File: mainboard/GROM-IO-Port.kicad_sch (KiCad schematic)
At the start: 27 parts, among them J13 I/O Port, J14 GROM Port, U14 74LS00, U15 74LS04, U18 74LS00, U20 74LS04, U3 74LS04, U4 74LS32, U45 74LS244, U46 74LS367, U47 74LS367

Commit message: PCB routed
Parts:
- added J13: I/O Port, Connector_PinHeader_2.54mm:PinHeader_2x22_P2.54mm_Vertical, symbol Connector_Generic:Conn_02x22_Odd_Even
- added J16: GROM Port, Connector_PinHeader_2.54mm:PinHeader_2x18_P2.54mm_Vertical, symbol Connector_Generic:Conn_02x18_Odd_Even
- J14: renamed from J13; footprint (none) -> Library:CardEdge_44Pin_2.54mm_Vertical
- J15: renamed from J14; footprint (none) -> Library:CardEdge_34Pin_2.54mm_Vertical
- U14, U15, U18, U20, U3, U4: footprint Package_DIP:DIP-14_W7.62mm_LongPads -> Package_DIP:DIP-14_W7.62mm_Socket_LongPads
- U44: renamed from U45; footprint Package_DIP:DIP-20_W7.62mm_LongPads -> Package_DIP:DIP-20_W7.62mm_Socket_LongPads
- U45: renamed from U46; footprint Package_DIP:DIP-16_W7.62mm_LongPads -> Package_DIP:DIP-16_W7.62mm_Socket_LongPads
- U46: renamed from U47; footprint Package_DIP:DIP-16_W7.62mm_LongPads -> Package_DIP:DIP-16_W7.62mm_Socket_LongPads
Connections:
- net +5V: now also J13.1 (Pin_1), J16.19 (Pin_19)
- net -5V: now also J13.43 (Pin_43), J16.29 (Pin_29)
- net A10: now also J16.16 (Pin_16)
- net A11: now also J16.14 (Pin_14)
- net A12: now also J16.12 (Pin_12)
- net A13: now also J16.10 (Pin_10)
- net A15-CRUOUT: now also J16.8 (Pin_8)
- net A3: now also J16.24 (Pin_24)
- net A4: now also J16.30 (Pin_30)
- net A5: now also J16.28 (Pin_28)
- net A6: now also J16.26 (Pin_26)
- net A7: now also J16.22 (Pin_22)
- net A8: now also J16.20 (Pin_20)
- net A9: now also J16.18 (Pin_18)
- net CRUIN: now also J16.6 (Pin_6)
- net D0: now also J13.37 (Pin_37), J16.17 (Pin_17)
- net D1: now also J13.40 (Pin_40), J16.15 (Pin_15)
- net D2: now also J13.39 (Pin_39), J16.13 (Pin_13)
- net D3: now also J13.42 (Pin_42), J16.11 (Pin_11)
- net D4: now also J13.35 (Pin_35), J16.9 (Pin_9)
- net D5: now also J13.38 (Pin_38), J16.7 (Pin_7)
- net D6: now also J13.36 (Pin_36), J16.5 (Pin_5)
- net D7: now also J13.34 (Pin_34), J16.3 (Pin_3)
- net DBIN: now also J16.25 (Pin_25)
- net GND: now also J13.21 (Pin_21), J13.23 (Pin_23), J13.25 (Pin_25), J13.27 (Pin_27), J16.2 (Pin_2), J16.35 (Pin_35), J16.36 (Pin_36)
- net GREADY: now also J16.31 (Pin_31)
- net GRMCLK: now also J16.27 (Pin_27)
- net IO_A0: now also J13.31 (Pin_31)
- net IO_A1: now also J13.30 (Pin_30)
- net IO_A10: now also J13.6 (Pin_6)
- net IO_A11: now also J13.8 (Pin_8)
- net IO_A12: now also J13.11 (Pin_11)
- net IO_A13: now also J13.15 (Pin_15)
- net IO_A14: now also J13.16 (Pin_16), J16.23 (Pin_23)
- net IO_A15-CRUOUT: now also J13.19 (Pin_19)
- net IO_A2: now also J13.20 (Pin_20)
- net IO_A3: now also J13.10 (Pin_10)
- net IO_A4: now also J13.7 (Pin_7)
- net IO_A5: now also J13.5 (Pin_5)
- net IO_A6: now also J13.29 (Pin_29)
- net IO_A7: now also J13.17 (Pin_17)
- net IO_A8: now also J13.14 (Pin_14)
- net IO_A9: now also J13.18 (Pin_18)
- net IO_CRUIN: now also J13.33 (Pin_33)
- net IO_DBIN: now also J13.9 (Pin_9)
- net IO_Ø3: now also J13.24 (Pin_24)
- net READY_~{HOLD}: now also J13.12 (Pin_12)
- net SBE: now also J13.2 (Pin_2)
- net VSS: now also J16.33 (Pin_33)
- net ~{CMRESET}: now also J16.1 (Pin_1)
- net ~{CRUCLK}: now also J16.4 (Pin_4)
- net ~{GS}: now also J16.21 (Pin_21)
- net ~{IO_CRUCLK}: now also J13.22 (Pin_22)
- net ~{IO_EXT_INT}: now also J13.4 (Pin_4)
- net ~{IO_LOAD}: now also J13.13 (Pin_13)
- net ~{IO_MBE}: now also J13.28 (Pin_28)
- net ~{IO_RESET}: now also J13.3 (Pin_3)
- net ~{IO_WE}: now also J13.26 (Pin_26)
- net ~{MEMEN}: now also J13.32 (Pin_32)
- net ~{ROMG}: now also J16.34 (Pin_34)
- net ~{mWE}: now also J16.32 (Pin_32)
- net IO_SNDIN: now reaches J14.44 (Pin_44), R103.1
- net IO_SNDIN: now also J13.44 (Pin_44)
- new net HOLD/IAQ: J13.41 (Pin_41)
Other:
- moved on the sheet: U45, U46

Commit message: unicorn work
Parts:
- renumbered R104 to R100, R89 to R85, R90 to R86, R91 to R87, R92 to R88, R93 to R89, R94 to R90, R95 to R91, R96 to R92, R97 to R93, R98 to R94, R99 to R95, R100 to R96, R101 to R97, R102 to R98, R103 to R99, U44 to U40, U45 to U41, U46 to U42

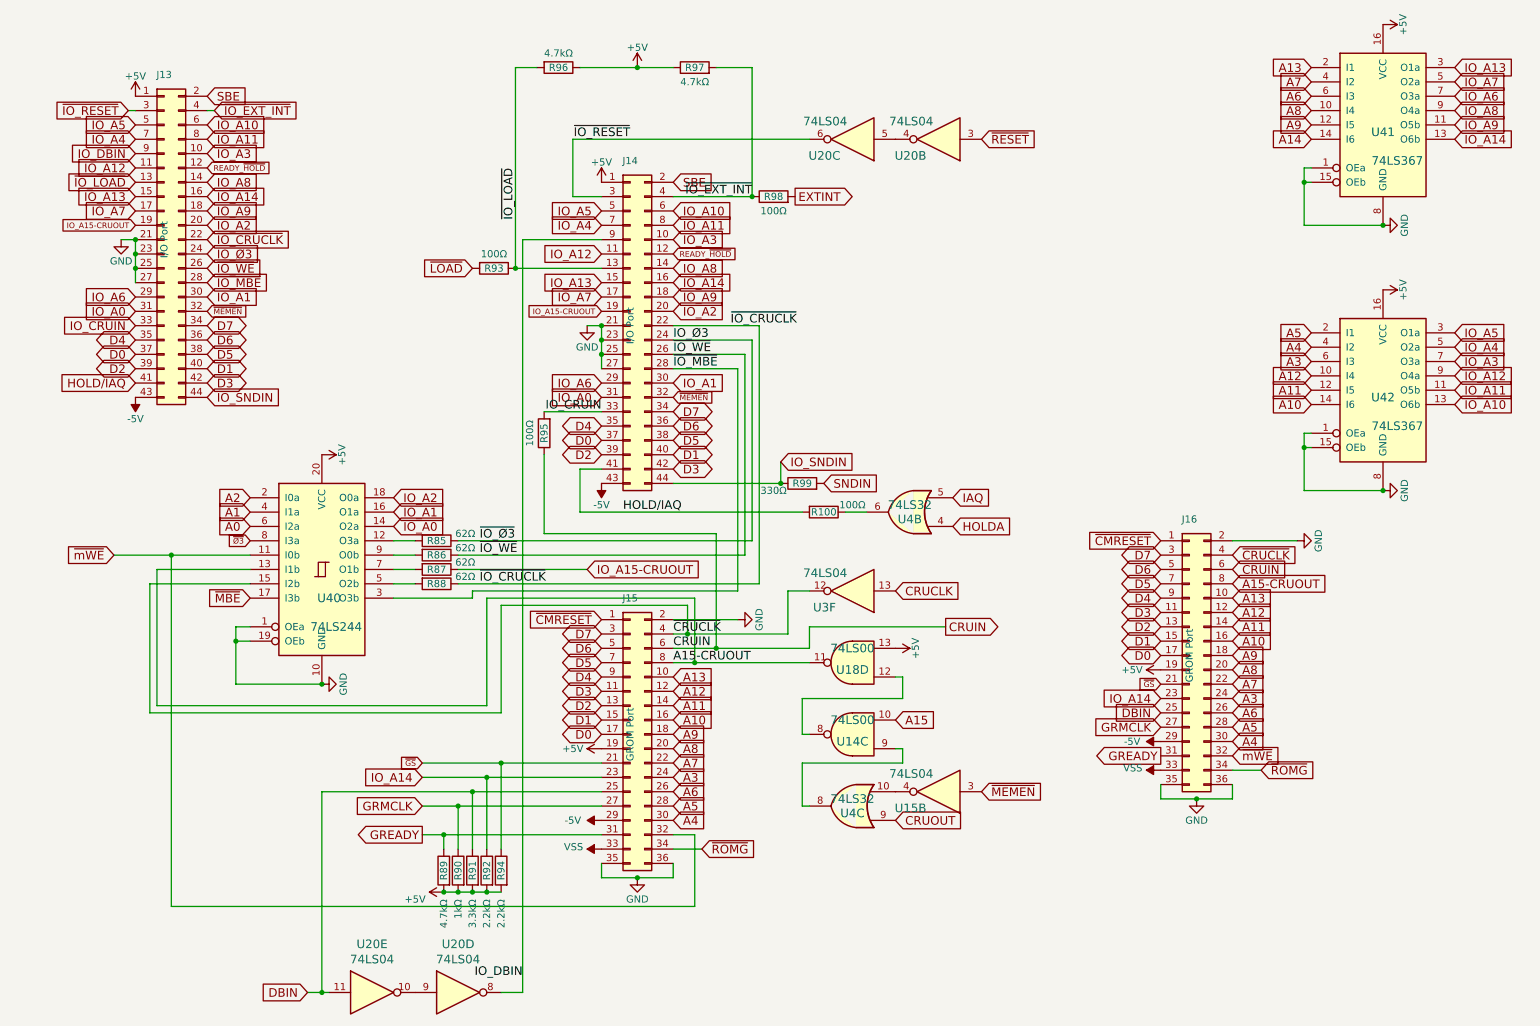
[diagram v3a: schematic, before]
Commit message: Shrink PCB
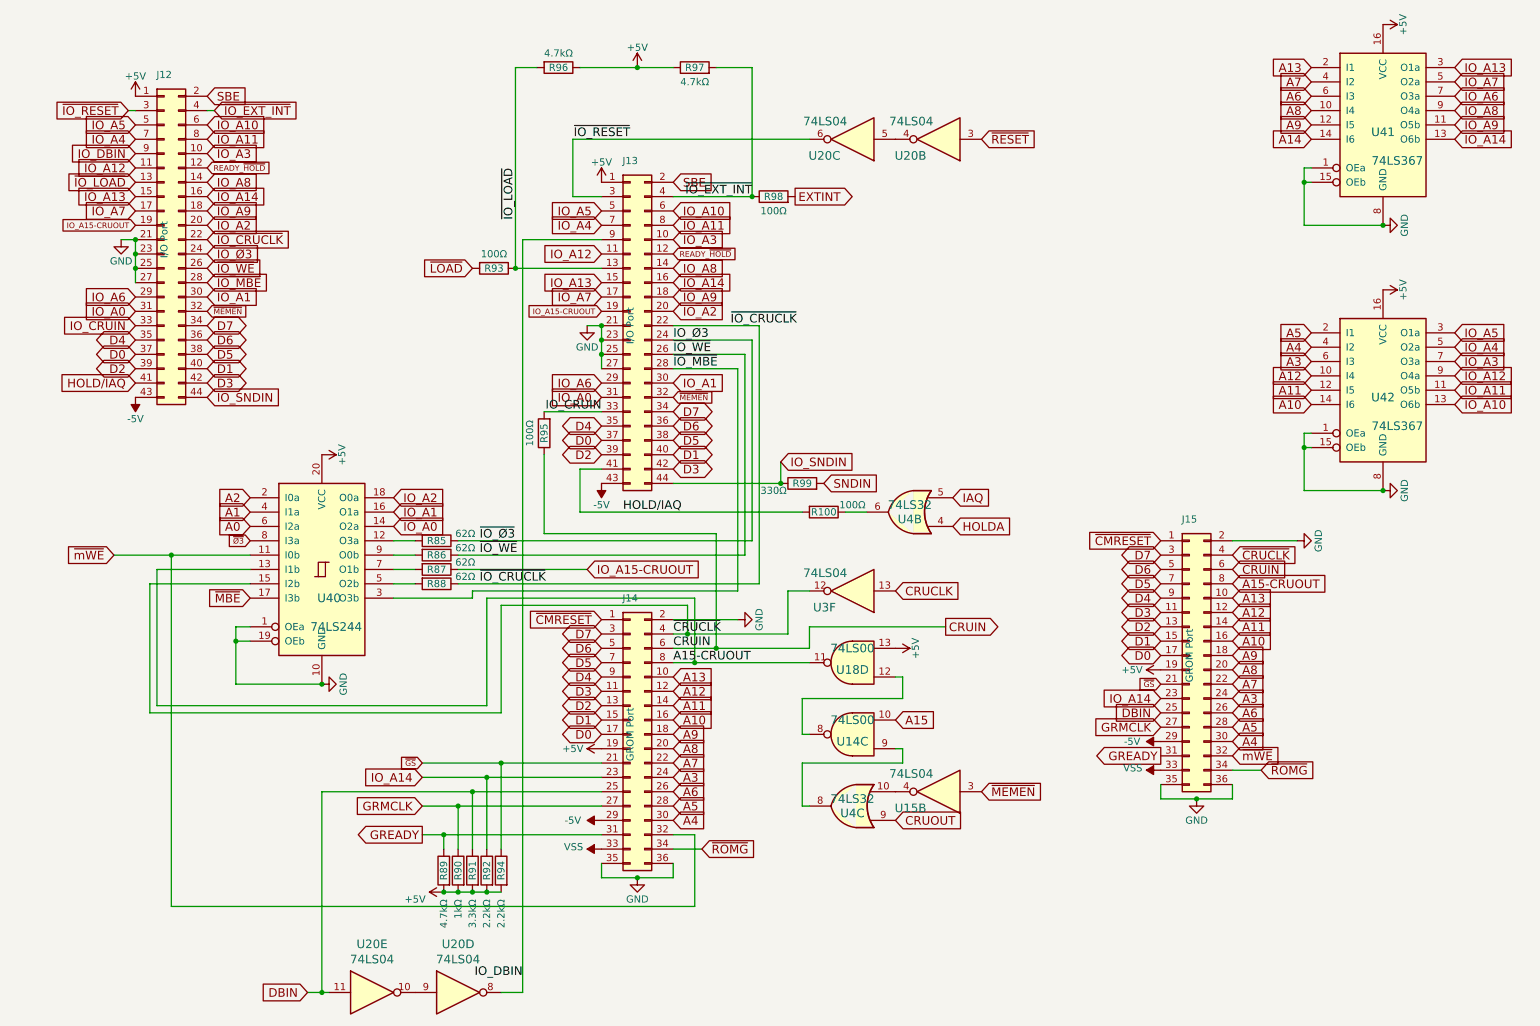
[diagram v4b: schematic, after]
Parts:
- renumbered J13 to J12, J14 to J13, J15 to J14, J16 to J15
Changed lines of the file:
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@@
   (symbol (lib_id "Connector_Generic:Conn_02x22_Odd_Even") (at 123.19 69.85 0) (unit 1)
     (in_bom yes) (on_board yes)
-    (property "Reference" "J14" (id 0) (at 123.19 40.64 0))
+    (property "Reference" "J13" (id 0) (at 123.19 40.64 0))
     (property "Value" "I/O Port" (id 1) (at 123.19 69.85 90))
     (property "Footprint" "Library:CardEdge_44Pin_2.54mm_Vertical" (id 2) (at 123.19 92.71 0)
@@
   (symbol (lib_id "Connector_Generic:Conn_02x18_Odd_Even") (at 123.19 142.24 0) (unit 1)
     (in_bom yes) (on_board yes)
-    (property "Reference" "J15" (id 0) (at 123.19 118.11 0))
+    (property "Reference" "J14" (id 0) (at 123.19 118.11 0))
     (property "Value" "GROM Port" (id 1) (at 123.19 142.24 90))
     (property "Footprint" "Library:CardEdge_34Pin_2.54mm_Vertical" (id 2) (at 123.19 168.91 0)
@@
   (symbol (lib_id "Connector_Generic:Conn_02x22_Odd_Even") (at 40.64 54.61 0) (unit 1)
     (in_bom yes) (on_board yes)
-    (property "Reference" "J13" (id 0) (at 40.64 25.4 0))
+    (property "Reference" "J12" (id 0) (at 40.64 25.4 0))
     (property "Value" "I/O Port" (id 1) (at 40.64 54.61 90))
     (property "Footprint" "Connector_PinHeader_2.54mm:PinHeader_2x22_P2.54mm_Vertical" (id 2) (at 40.64 77.47 0)
@@
   (symbol (lib_id "Connector_Generic:Conn_02x18_Odd_Even") (at 222.25 128.27 0) (unit 1)
     (in_bom yes) (on_board yes)
-    (property "Reference" "J16" (id 0) (at 222.25 104.14 0))
+    (property "Reference" "J15" (id 0) (at 222.25 104.14 0))
     (property "Value" "GROM Port" (id 1) (at 222.25 128.27 90))
     (property "Footprint" "Connector_PinHeader_2.54mm:PinHeader_2x18_P2.54mm_Vertical" (id 2) (at 222.25 154.94 0)

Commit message: hardware updates
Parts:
- J13: footprint Library:CardEdge_44Pin_2.54mm_Vertical -> WernerCustomLibrary:44 Pin Card Edge
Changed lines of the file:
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@@
     (property "Reference" "J13" (id 0) (at 123.19 40.64 0))
     (property "Value" "I/O Port" (id 1) (at 123.19 69.85 90))
-    (property "Footprint" "Library:CardEdge_44Pin_2.54mm_Vertical" (id 2) (at 123.19 92.71 0)
+    (property "Footprint" "WernerCustomLibrary:44 Pin Card Edge" (id 2) (at 123.19 92.71 0)
       (effects (font (size 1.524 1.524)) hide)
     )

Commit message: hardware updates
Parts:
- renumbered R85 to R84, R86 to R85, R87 to R86, R88 to R87, R89 to R88, R90 to R89, R91 to R90, R92 to R91, R93 to R92, R94 to R93, R95 to R94, R96 to R95, R97 to R96, R98 to R97, R99 to R98, R100 to R99
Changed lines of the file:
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@@
   (symbol (lib_id "Console-rescue:R") (at 88.9 115.57 270) (unit 1)
     (in_bom yes) (on_board yes)
-    (property "Reference" "R88" (id 0) (at 88.9 115.57 90))
+    (property "Reference" "R87" (id 0) (at 88.9 115.57 90))
     (property "Value" "62Ω" (id 1) (at 93.98 114.3 90))
     (property "Footprint" "Resistor_THT:R_Axial_DIN0207_L6.3mm_D2.5mm_P7.62mm_Horizontal" (id 2) (at 88.9 113.792 90)
@@
   (symbol (lib_id "Console-rescue:R") (at 88.9 110.49 270) (unit 1)
     (in_bom yes) (on_board yes)
-    (property "Reference" "R86" (id 0) (at 88.9 110.49 90))
+    (property "Reference" "R85" (id 0) (at 88.9 110.49 90))
     (property "Value" "62Ω" (id 1) (at 93.98 109.22 90))
     (property "Footprint" "Resistor_THT:R_Axial_DIN0207_L6.3mm_D2.5mm_P7.62mm_Horizontal" (id 2) (at 88.9 108.712 90)
@@
   (symbol (lib_id "Console-rescue:R") (at 88.9 107.95 270) (unit 1)
     (in_bom yes) (on_board yes)
-    (property "Reference" "R85" (id 0) (at 88.9 107.95 90))
+    (property "Reference" "R84" (id 0) (at 88.9 107.95 90))
     (property "Value" "62Ω" (id 1) (at 93.98 106.68 90))
     (property "Footprint" "Resistor_THT:R_Axial_DIN0207_L6.3mm_D2.5mm_P7.62mm_Horizontal" (id 2) (at 88.9 106.172 90)
@@
   (symbol (lib_id "Console-rescue:R") (at 88.9 113.03 270) (unit 1)
     (in_bom yes) (on_board yes)
-    (property "Reference" "R87" (id 0) (at 88.9 113.03 90))
+    (property "Reference" "R86" (id 0) (at 88.9 113.03 90))
     (property "Value" "62Ω" (id 1) (at 93.98 111.76 90))
     (property "Footprint" "Resistor_THT:R_Axial_DIN0207_L6.3mm_D2.5mm_P7.62mm_Horizontal" (id 2) (at 88.9 111.252 90)
@@
   (symbol (lib_id "Console-rescue:R") (at 97.79 166.37 0) (mirror y) (unit 1)
     (in_bom yes) (on_board yes)
-    (property "Reference" "R92" (id 0) (at 97.79 166.37 90))
+    (property "Reference" "R91" (id 0) (at 97.79 166.37 90))
     (property "Value" "2.2kΩ" (id 1) (at 97.79 171.45 90)
       (effects (font (size 1.27 1.27)) (justify right))
@@
   (symbol (lib_id "Console-rescue:R") (at 95.25 166.37 0) (mirror y) (unit 1)
     (in_bom yes) (on_board yes)
-    (property "Reference" "R91" (id 0) (at 95.25 166.37 90))
+    (property "Reference" "R90" (id 0) (at 95.25 166.37 90))
     (property "Value" "3.3kΩ" (id 1) (at 95.25 171.45 90)
       (effects (font (size 1.27 1.27)) (justify right))
@@
   (symbol (lib_id "Console-rescue:R") (at 92.71 166.37 0) (mirror y) (unit 1)
     (in_bom yes) (on_board yes)
-    (property "Reference" "R90" (id 0) (at 92.71 166.37 90))
+    (property "Reference" "R89" (id 0) (at 92.71 166.37 90))
     (property "Value" "1kΩ" (id 1) (at 92.71 171.45 90)
       (effects (font (size 1.27 1.27)) (justify right))
@@
   (symbol (lib_id "Console-rescue:R") (at 90.17 166.37 0) (mirror y) (unit 1)
     (in_bom yes) (on_board yes)
-    (property "Reference" "R89" (id 0) (at 90.17 166.37 90))
+    (property "Reference" "R88" (id 0) (at 90.17 166.37 90))
     (property "Value" "4.7kΩ" (id 1) (at 90.17 171.45 90)
       (effects (font (size 1.27 1.27)) (justify right))
@@
   (symbol (lib_id "Console-rescue:R") (at 100.33 166.37 0) (mirror y) (unit 1)
     (in_bom yes) (on_board yes)
-    (property "Reference" "R94" (id 0) (at 100.33 166.37 90))
+    (property "Reference" "R93" (id 0) (at 100.33 166.37 90))
     (property "Value" "2.2kΩ" (id 1) (at 100.33 171.45 90)
       (effects (font (size 1.27 1.27)) (justify right))
@@
   (symbol (lib_id "Console-rescue:R") (at 107.95 88.9 180) (unit 1)
     (in_bom yes) (on_board yes)
-    (property "Reference" "R95" (id 0) (at 107.95 88.9 90))
+    (property "Reference" "R94" (id 0) (at 107.95 88.9 90))
     (property "Value" "100Ω" (id 1) (at 105.41 88.9 90))
     (property "Footprint" "Resistor_THT:R_Axial_DIN0207_L6.3mm_D2.5mm_P7.62mm_Horizontal" (id 2) (at 109.728 88.9 90)
@@
   (symbol (lib_id "Console-rescue:R") (at 148.59 46.99 90) (unit 1)
     (in_bom yes) (on_board yes)
-    (property "Reference" "R98" (id 0) (at 148.59 46.99 90))
+    (property "Reference" "R97" (id 0) (at 148.59 46.99 90))
     (property "Value" "100Ω" (id 1) (at 148.59 49.53 90))
     (property "Footprint" "Resistor_THT:R_Axial_DIN0207_L6.3mm_D2.5mm_P7.62mm_Horizontal" (id 2) (at 148.59 48.768 90)
@@
   (symbol (lib_id "Console-rescue:R") (at 134.62 24.13 90) (unit 1)
     (in_bom yes) (on_board yes)
-    (property "Reference" "R97" (id 0) (at 134.62 24.13 90))
+    (property "Reference" "R96" (id 0) (at 134.62 24.13 90))
     (property "Value" "4.7kΩ" (id 1) (at 134.62 26.67 90))
     (property "Footprint" "Resistor_THT:R_Axial_DIN0207_L6.3mm_D2.5mm_P7.62mm_Horizontal" (id 2) (at 134.62 25.908 90)
@@
   (symbol (lib_id "Console-rescue:R") (at 99.06 59.69 270) (unit 1)
     (in_bom yes) (on_board yes)
-    (property "Reference" "R93" (id 0) (at 99.06 59.69 90))
+    (property "Reference" "R92" (id 0) (at 99.06 59.69 90))
     (property "Value" "100Ω" (id 1) (at 99.06 57.15 90))
     (property "Footprint" "Resistor_THT:R_Axial_DIN0207_L6.3mm_D2.5mm_P7.62mm_Horizontal" (id 2) (at 99.06 57.912 90)
@@
   (symbol (lib_id "Console-rescue:R") (at 110.49 24.13 270) (unit 1)
     (in_bom yes) (on_board yes)
-    (property "Reference" "R96" (id 0) (at 110.49 24.13 90))
+    (property "Reference" "R95" (id 0) (at 110.49 24.13 90))
     (property "Value" "4.7kΩ" (id 1) (at 110.49 21.59 90))
     (property "Footprint" "Resistor_THT:R_Axial_DIN0207_L6.3mm_D2.5mm_P7.62mm_Horizontal" (id 2) (at 110.49 22.352 90)
@@
   (symbol (lib_id "Console-rescue:R") (at 157.48 102.87 270) (unit 1)
     (in_bom yes) (on_board yes)
-    (property "Reference" "R100" (id 0) (at 157.48 102.87 90))
+    (property "Reference" "R99" (id 0) (at 157.48 102.87 90))
     (property "Value" "100Ω" (id 1) (at 162.56 101.6 90))
     (property "Footprint" "Resistor_THT:R_Axial_DIN0207_L6.3mm_D2.5mm_P7.62mm_Horizontal" (id 2) (at 157.48 101.092 90)
@@
   (symbol (lib_id "Console-rescue:R") (at 153.67 97.79 90) (unit 1)
     (in_bom yes) (on_board yes)
-    (property "Reference" "R99" (id 0) (at 153.67 97.79 90))
+    (property "Reference" "R98" (id 0) (at 153.67 97.79 90))
     (property "Value" "330Ω" (id 1) (at 148.59 99.06 90))
     (property "Footprint" "Resistor_THT:R_Axial_DIN0207_L6.3mm_D2.5mm_P7.62mm_Horizontal" (id 2) (at 153.67 99.568 90)

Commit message: PCB cleanup
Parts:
- R84, R85, R86, R87, R88, R89, R90, R91, R92, R93, R94, R95, R96, R97, R98, R99: symbol Console-rescue:R -> Device:R

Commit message: PCB rework
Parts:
- renumbered R84 to R41, R85 to R42, R86 to R43, R87 to R44, R88 to R45, R89 to R46, R90 to R47, R91 to R48, R92 to R49, R93 to R50, R94 to R51, R95 to R52, R96 to R53, R97 to R54, R98 to R55, R99 to R56, U20 to U22, U40 to U41, U41 to U42, U42 to U43
